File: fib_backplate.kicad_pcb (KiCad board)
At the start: 2 copper layers, 106.7 x 92.7 mm, 32 parts

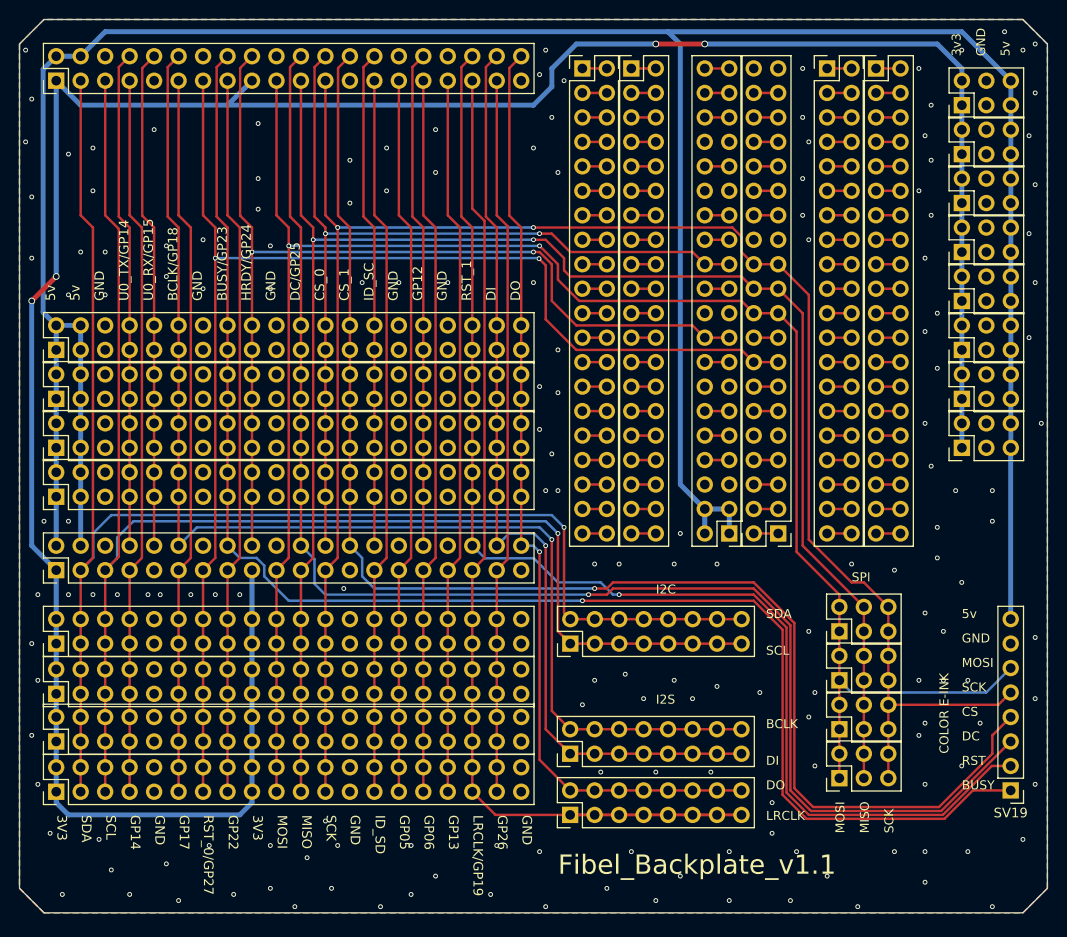
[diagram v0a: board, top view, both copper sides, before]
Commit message: moved eink connector slightly to the side, ready for fabrication v1.1
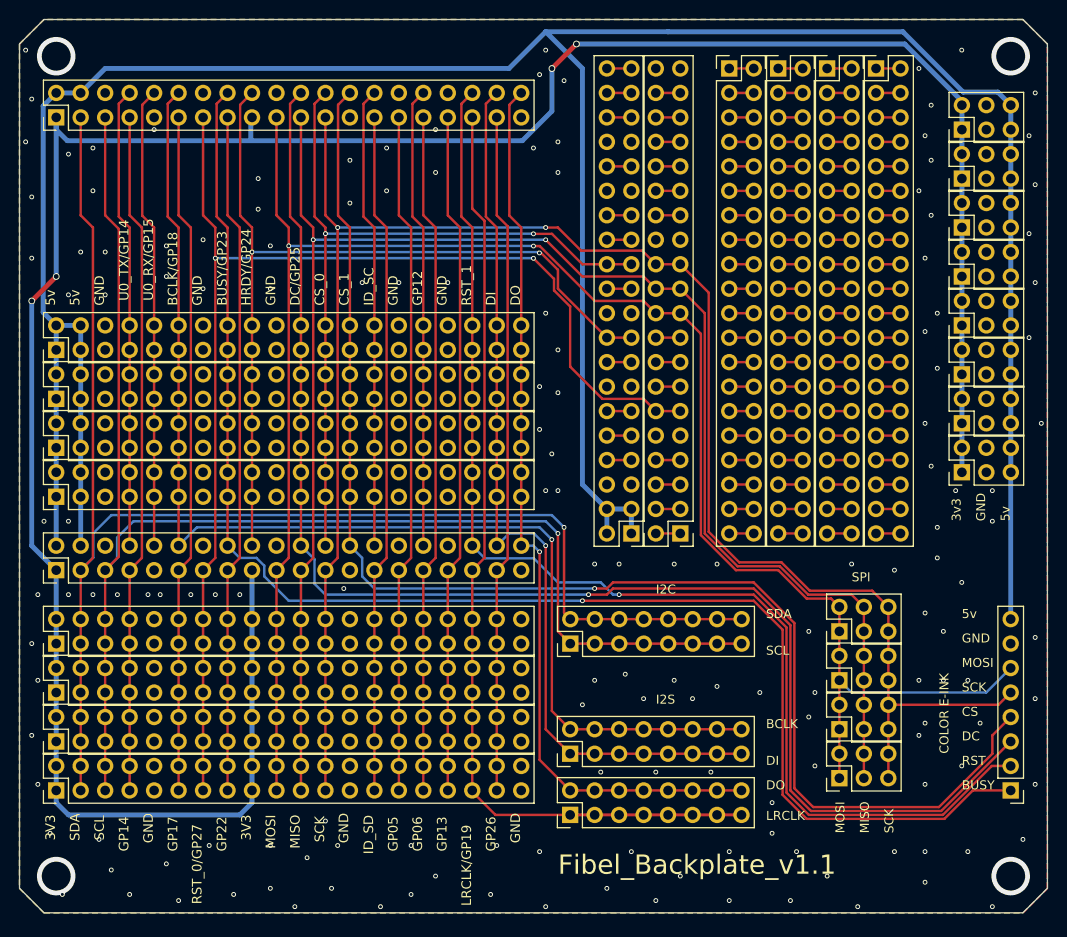
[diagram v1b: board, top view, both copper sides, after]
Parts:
- moved SV20 15.2 mm to (149.9, 55.9)
- moved SV21 15.2 mm to (154.9, 55.9)
- moved SV7 10.2 mm to (139.7, 104.1)
- moved SV23 10.2 mm to (144.8, 104.1)
- moved SV1 3.81 mm to (80.0, 61.0)
- moved SV34 2.54 mm to (174.0, 97.8)
- moved SV39 2.54 mm to (174.0, 72.4)
- moved SV35 2.53 mm to (174.0, 92.7)
- moved SV36 2.53 mm to (174.0, 87.6)
- moved SV37 2.53 mm to (174.0, 82.5)
- moved SV38 2.53 mm to (174.0, 77.5)
- moved SV40 2.53 mm to (174.0, 67.3)
- moved SV41 2.53 mm to (174.0, 62.2)
- moved SV11 0.13 mm to (80.0, 130.8)
- moved SV13 0.13 mm to (80.0, 120.7)
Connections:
- SV23 pad 11: Net-(SV23-Pad11) -> /RST_0
- SV23 pad 12: Net-(SV23-Pad11) -> /RST_0
- SV23 pad 15: /RST_0 -> Net-(SV23-Pad15)
- SV23 pad 16: /RST_0 -> Net-(SV23-Pad15)
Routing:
- net /HRDY: track 107.3 -> 92.2 mm
- net /CS_0: track 95.0 -> 81.0 mm
- net /RST_0: track 141.0 -> 130.2 mm
- net /MOSI: track 199.7 -> 193.1 mm
- net /MISO: track 180.4 -> 175.1 mm
- net /SCK: track 195.1 -> 190.0 mm
- net /ID_SD: track 74.8 -> 71.0 mm
- net /GP22: track 74.8 -> 71.0 mm
- net /GP13: track 74.8 -> 71.0 mm
- net /GP06: track 74.8 -> 71.0 mm
- net /GP12: track 51.7 -> 47.9 mm
- net /U0_TX: track 51.7 -> 47.9 mm
- net /U0_RX: track 51.8 -> 48.0 mm
- net /SDA: track 157.0 -> 153.2 mm
- net /SCL: track 155.6 -> 151.8 mm
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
